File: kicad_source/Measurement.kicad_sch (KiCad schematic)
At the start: 21 parts, among them U10 ADS1015IDGS, U11 OPA2374AIDCN, U9 OPA2374AIDCN

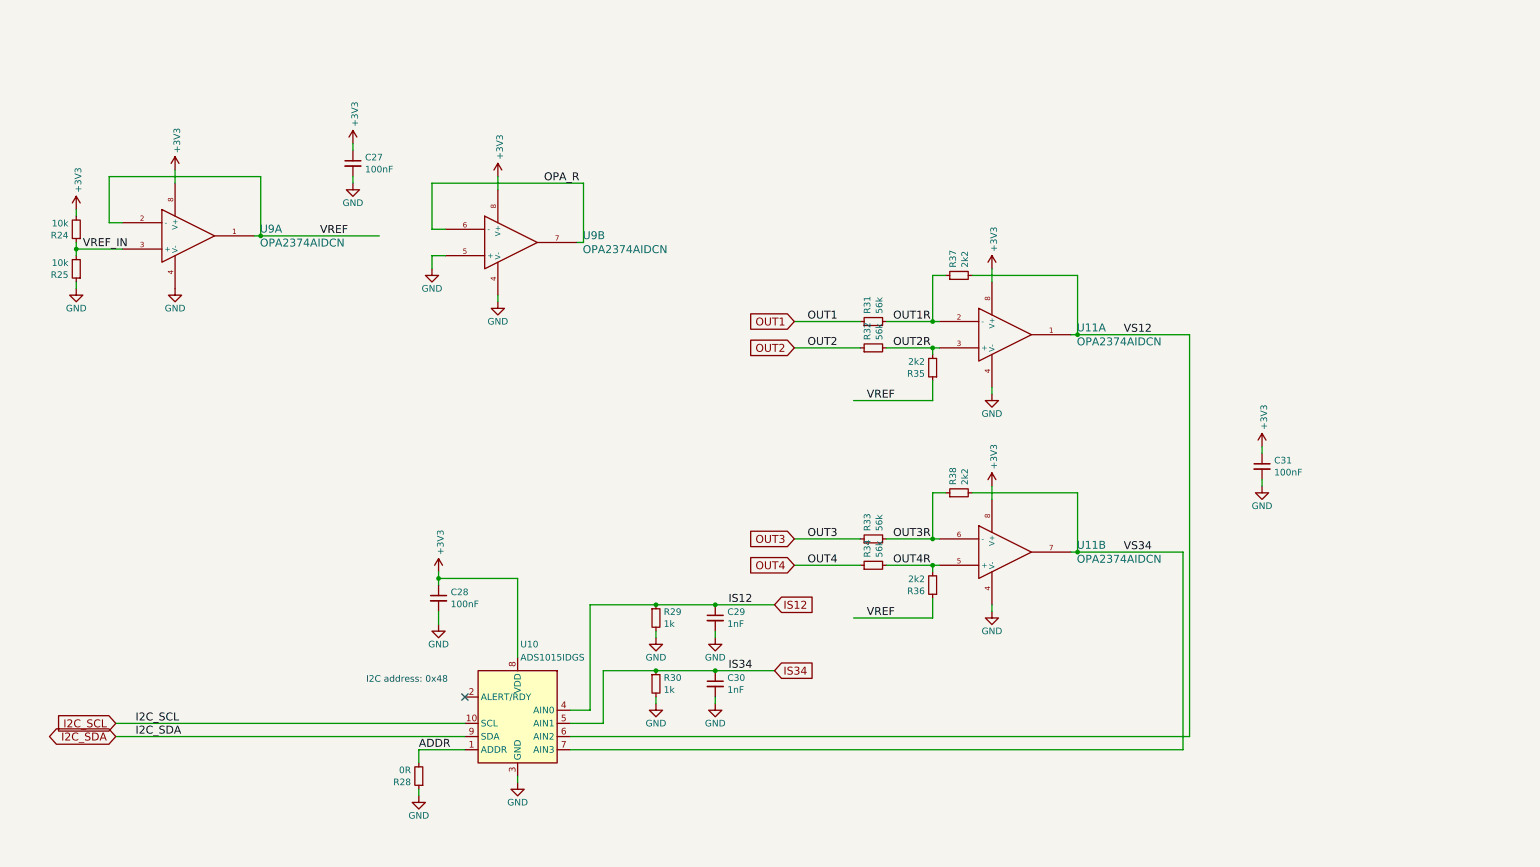
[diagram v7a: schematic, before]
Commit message: combined 3.3V nets
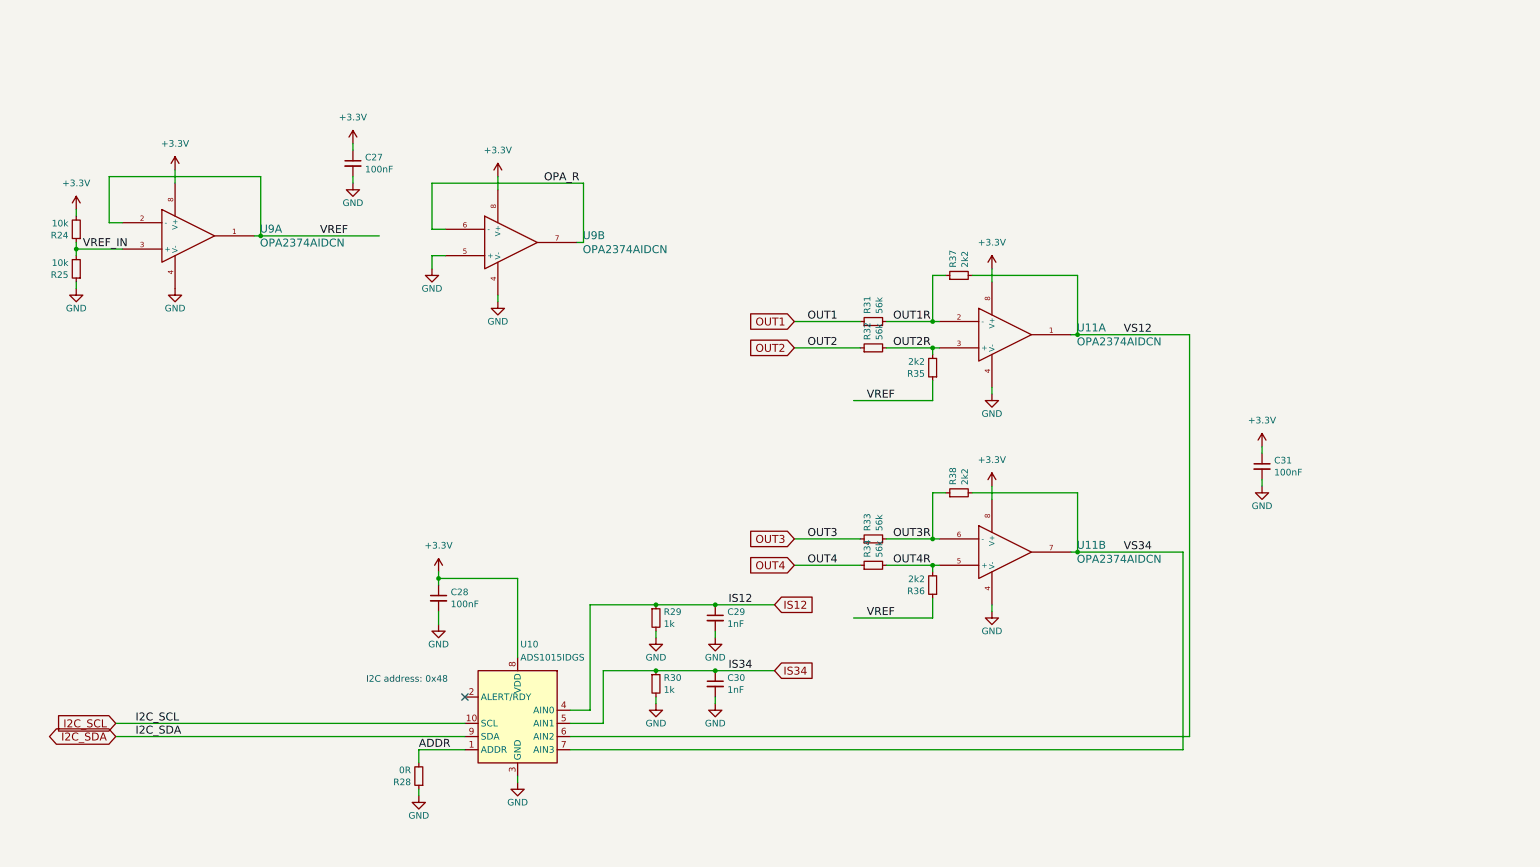
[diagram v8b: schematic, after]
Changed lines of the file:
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@@
   (title_block
     (title "CyphalRobotController07/CAN")
-    (date "2023-11-15")
-    (rev "0.1")
+    (date "2023-12-03")
+    (rev "0.2")
     (company "generationmake")
     (comment 4 "This documentation describes Open Hardware and is licensed under the CERN OHL v. 1.2.")
@@
     (property "Footprint" "" (id 2) (at 106.68 68.58 0))
     (property "Datasheet" "" (id 3) (at 106.68 68.58 0))
-    (pin "1")
-  )
-  (symbol (lib_id "power:+3.3V") (at 106.68 44.45 0) (unit 1)
-    (in_bom yes) (on_board yes)
-    (property "Reference" "#PWR082" (id 0) (at 106.68 48.26 0)
-      (effects (font (size 1.27 1.27)) hide)
-    )
-    (property "Value" "+3V3" (id 1) (at 107.061 41.1988 90)
-      (effects (font (size 1.27 1.27)) (justify left))
-    )
-    (property "Footprint" "" (id 2) (at 106.68 44.45 0))
-    (property "Datasheet" "" (id 3) (at 106.68 44.45 0))
     (pin "1")
   )
@@
     (pin "7")
   )
-  (symbol (lib_id "power:+3.3V") (at 44.45 43.18 0) (unit 1)
-    (in_bom yes) (on_board yes)
-    (property "Reference" "#PWR072" (id 0) (at 44.45 46.99 0)
-      (effects (font (size 1.27 1.27)) hide)
-    )
-    (property "Value" "+3V3" (id 1) (at 44.831 39.9288 90)
-      (effects (font (size 1.27 1.27)) (justify left))
-    )
-    (property "Footprint" "" (id 2) (at 44.45 43.18 0))
-    (property "Datasheet" "" (id 3) (at 44.45 43.18 0))
-    (pin "1")
-  )
   (symbol (lib_id "power:GND") (at 44.45 66.04 0) (unit 1)
     (in_bom yes) (on_board yes)
@@
     (pin "1")
   )
-  (symbol (lib_id "power:+3.3V") (at 25.4 50.8 0) (unit 1)
-    (in_bom yes) (on_board yes)
-    (property "Reference" "#PWR070" (id 0) (at 25.4 54.61 0)
-      (effects (font (size 1.27 1.27)) hide)
-    )
-    (property "Value" "+3V3" (id 1) (at 25.781 47.5488 90)
-      (effects (font (size 1.27 1.27)) (justify left))
-    )
-    (property "Footprint" "" (id 2) (at 25.4 50.8 0))
-    (property "Datasheet" "" (id 3) (at 25.4 50.8 0))
-    (pin "1")
-  )
   (symbol (lib_id "Device:R_Small") (at 190.5 81.28 180) (unit 1)
     (in_bom yes) (on_board yes)
@@
     (pin "1")
   )
-  (symbol (lib_id "power:+3.3V") (at 95.25 120.65 0) (unit 1)
-    (in_bom yes) (on_board yes)
-    (property "Reference" "#PWR080" (id 0) (at 95.25 124.46 0)
-      (effects (font (size 1.27 1.27)) hide)
-    )
-    (property "Value" "+3V3" (id 1) (at 95.631 117.3988 90)
-      (effects (font (size 1.27 1.27)) (justify left))
-    )
-    (property "Footprint" "" (id 2) (at 95.25 120.65 0))
-    (property "Datasheet" "" (id 3) (at 95.25 120.65 0))
-    (pin "1")
-  )
   (symbol (lib_id "Device:C_Small") (at 78.74 41.91 0) (unit 1)
     (in_bom yes) (on_board yes)
@@
     (pin "1")
     (pin "2")
-  )
-  (symbol (lib_id "power:+3.3V") (at 78.74 38.1 0) (unit 1)
-    (in_bom yes) (on_board yes)
-    (property "Reference" "#PWR076" (id 0) (at 78.74 41.91 0)
-      (effects (font (size 1.27 1.27)) hide)
-    )
-    (property "Value" "+3V3" (id 1) (at 79.121 34.8488 90)
-      (effects (font (size 1.27 1.27)) (justify left))
-    )
-    (property "Footprint" "" (id 2) (at 78.74 38.1 0))
-    (property "Datasheet" "" (id 3) (at 78.74 38.1 0))
-    (pin "1")
   )
   (symbol (lib_id "power:GND") (at 78.74 45.72 0) (unit 1)
@@
     (pin "1")
   )
-  (symbol (lib_id "power:+3.3V") (at 201.93 62.23 0) (unit 1)
-    (in_bom yes) (on_board yes)
-    (property "Reference" "#PWR089" (id 0) (at 201.93 66.04 0)
-      (effects (font (size 1.27 1.27)) hide)
-    )
-    (property "Value" "+3V3" (id 1) (at 202.311 58.9788 90)
-      (effects (font (size 1.27 1.27)) (justify left))
-    )
-    (property "Footprint" "" (id 2) (at 201.93 62.23 0))
-    (property "Datasheet" "" (id 3) (at 201.93 62.23 0))
-    (pin "1")
-  )
   (symbol (lib_id "power:GND") (at 201.93 86.36 0) (unit 1)
     (in_bom yes) (on_board yes)
@@
     (pin "2")
   )
-  (symbol (lib_id "power:+3.3V") (at 254 96.52 0) (unit 1)
-    (in_bom yes) (on_board yes)
-    (property "Reference" "#PWR093" (id 0) (at 254 100.33 0)
-      (effects (font (size 1.27 1.27)) hide)
-    )
-    (property "Value" "+3V3" (id 1) (at 254.381 93.2688 90)
-      (effects (font (size 1.27 1.27)) (justify left))
-    )
-    (property "Footprint" "" (id 2) (at 254 96.52 0))
-    (property "Datasheet" "" (id 3) (at 254 96.52 0))
-    (pin "1")
-  )
   (symbol (lib_id "power:GND") (at 254 104.14 0) (unit 1)
     (in_bom yes) (on_board yes)
@@
     (pin "2")
   )
-  (symbol (lib_id "power:+3.3V") (at 201.93 104.14 0) (unit 1)
-    (in_bom yes) (on_board yes)
-    (property "Reference" "#PWR091" (id 0) (at 201.93 107.95 0)
-      (effects (font (size 1.27 1.27)) hide)
-    )
-    (property "Value" "+3V3" (id 1) (at 202.311 100.8888 90)
-      (effects (font (size 1.27 1.27)) (justify left))
-    )
-    (property "Footprint" "" (id 2) (at 201.93 104.14 0))
-    (property "Datasheet" "" (id 3) (at 201.93 104.14 0))
-    (pin "1")
-  )
   (symbol (lib_id "power:GND") (at 201.93 128.27 0) (unit 1)
     (in_bom yes) (on_board yes)
@@
     (property "Footprint" "" (id 2) (at 148.59 133.35 0))
     (property "Datasheet" "" (id 3) (at 148.59 133.35 0))
+    (pin "1")
+  )
+  (symbol (lib_id "power:+3.3V") (at 201.93 62.23 0) (unit 1)
+    (in_bom yes) (on_board yes) (fields_autoplaced)
+    (property "Reference" "#PWR0151" (id 0) (at 201.93 66.04 0)
+      (effects (font (size 1.27 1.27)) hide)
+    )
+    (property "Value" "+3.3V" (id 1) (at 201.93 57.15 0))
+    (property "Footprint" "" (id 2) (at 201.93 62.23 0)
+      (effects (font (size 1.27 1.27)) hide)
+    )
+    (property "Datasheet" "" (id 3) (at 201.93 62.23 0)
+      (effects (font (size 1.27 1.27)) hide)
+    )
+    (pin "1")
+  )
+  (symbol (lib_id "power:+3.3V") (at 95.25 120.65 0) (unit 1)
+    (in_bom yes) (on_board yes) (fields_autoplaced)
+    (property "Reference" "#PWR0139" (id 0) (at 95.25 124.46 0)
+      (effects (font (size 1.27 1.27)) hide)
+    )
+    (property "Value" "+3.3V" (id 1) (at 95.25 115.57 0))
+    (property "Footprint" "" (id 2) (at 95.25 120.65 0)
+      (effects (font (size 1.27 1.27)) hide)
+    )
+    (property "Datasheet" "" (id 3) (at 95.25 120.65 0)
+      (effects (font (size 1.27 1.27)) hide)
+    )
+    (pin "1")
+  )
+  (symbol (lib_id "power:+3.3V") (at 201.93 104.14 0) (unit 1)
+    (in_bom yes) (on_board yes) (fields_autoplaced)
+    (property "Reference" "#PWR0140" (id 0) (at 201.93 107.95 0)
+      (effects (font (size 1.27 1.27)) hide)
+    )
+    (property "Value" "+3.3V" (id 1) (at 201.93 99.06 0))
+    (property "Footprint" "" (id 2) (at 201.93 104.14 0)
+      (effects (font (size 1.27 1.27)) hide)
+    )
+    (property "Datasheet" "" (id 3) (at 201.93 104.14 0)
+      (effects (font (size 1.27 1.27)) hide)
+    )
+    (pin "1")
+  )
+  (symbol (lib_id "power:+3.3V") (at 106.68 44.45 0) (unit 1)
+    (in_bom yes) (on_board yes) (fields_autoplaced)
+    (property "Reference" "#PWR0150" (id 0) (at 106.68 48.26 0)
+      (effects (font (size 1.27 1.27)) hide)
+    )
+    (property "Value" "+3.3V" (id 1) (at 106.68 39.37 0))
+    (property "Footprint" "" (id 2) (at 106.68 44.45 0)
+      (effects (font (size 1.27 1.27)) hide)
+    )
+    (property "Datasheet" "" (id 3) (at 106.68 44.45 0)
+      (effects (font (size 1.27 1.27)) hide)
+    )
+    (pin "1")
+  )
+  (symbol (lib_id "power:+3.3V") (at 254 96.52 0) (unit 1)
+    (in_bom yes) (on_board yes) (fields_autoplaced)
+    (property "Reference" "#PWR0141" (id 0) (at 254 100.33 0)
+      (effects (font (size 1.27 1.27)) hide)
+    )
+    (property "Value" "+3.3V" (id 1) (at 254 91.44 0))
+    (property "Footprint" "" (id 2) (at 254 96.52 0)
+      (effects (font (size 1.27 1.27)) hide)
+    )
+    (property "Datasheet" "" (id 3) (at 254 96.52 0)
+      (effects (font (size 1.27 1.27)) hide)
+    )
+    (pin "1")
+  )
+  (symbol (lib_id "power:+3.3V") (at 78.74 38.1 0) (unit 1)
+    (in_bom yes) (on_board yes) (fields_autoplaced)
+    (property "Reference" "#PWR0146" (id 0) (at 78.74 41.91 0)
+      (effects (font (size 1.27 1.27)) hide)
+    )
+    (property "Value" "+3.3V" (id 1) (at 78.74 33.02 0))
+    (property "Footprint" "" (id 2) (at 78.74 38.1 0)
+      (effects (font (size 1.27 1.27)) hide)
+    )
+    (property "Datasheet" "" (id 3) (at 78.74 38.1 0)
+      (effects (font (size 1.27 1.27)) hide)
+    )
+    (pin "1")
+  )
+  (symbol (lib_id "power:+3.3V") (at 44.45 43.18 0) (unit 1)
+    (in_bom yes) (on_board yes) (fields_autoplaced)
+    (property "Reference" "#PWR0149" (id 0) (at 44.45 46.99 0)
+      (effects (font (size 1.27 1.27)) hide)
+    )
+    (property "Value" "+3.3V" (id 1) (at 44.45 38.1 0))
+    (property "Footprint" "" (id 2) (at 44.45 43.18 0)
+      (effects (font (size 1.27 1.27)) hide)
+    )
+    (property "Datasheet" "" (id 3) (at 44.45 43.18 0)
+      (effects (font (size 1.27 1.27)) hide)
+    )
     (pin "1")
   )
@@
     (pin "1")
   )
+  (symbol (lib_id "power:+3.3V") (at 25.4 50.8 0) (unit 1)
+    (in_bom yes) (on_board yes) (fields_autoplaced)
+    (property "Reference" "#PWR0148" (id 0) (at 25.4 54.61 0)
+      (effects (font (size 1.27 1.27)) hide)
+    )
+    (property "Value" "+3.3V" (id 1) (at 25.4 45.72 0))
+    (property "Footprint" "" (id 2) (at 25.4 50.8 0)
+      (effects (font (size 1.27 1.27)) hide)
+    )
+    (property "Datasheet" "" (id 3) (at 25.4 50.8 0)
+      (effects (font (size 1.27 1.27)) hide)
+    )
+    (pin "1")
+  )
